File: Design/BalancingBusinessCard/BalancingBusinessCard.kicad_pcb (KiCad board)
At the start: 2 copper layers, 51 x 89 mm, 31 parts, among them J101 TestPoints, M201 Motor_DC, U101 ATtiny261-20SU, U201 AP1017AEN, U401 LIS3DHTR, U501 FT440CA

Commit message: Final from Saturday
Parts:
- U401: value LIS3DHTR -> LGA-16_3x3x1mm

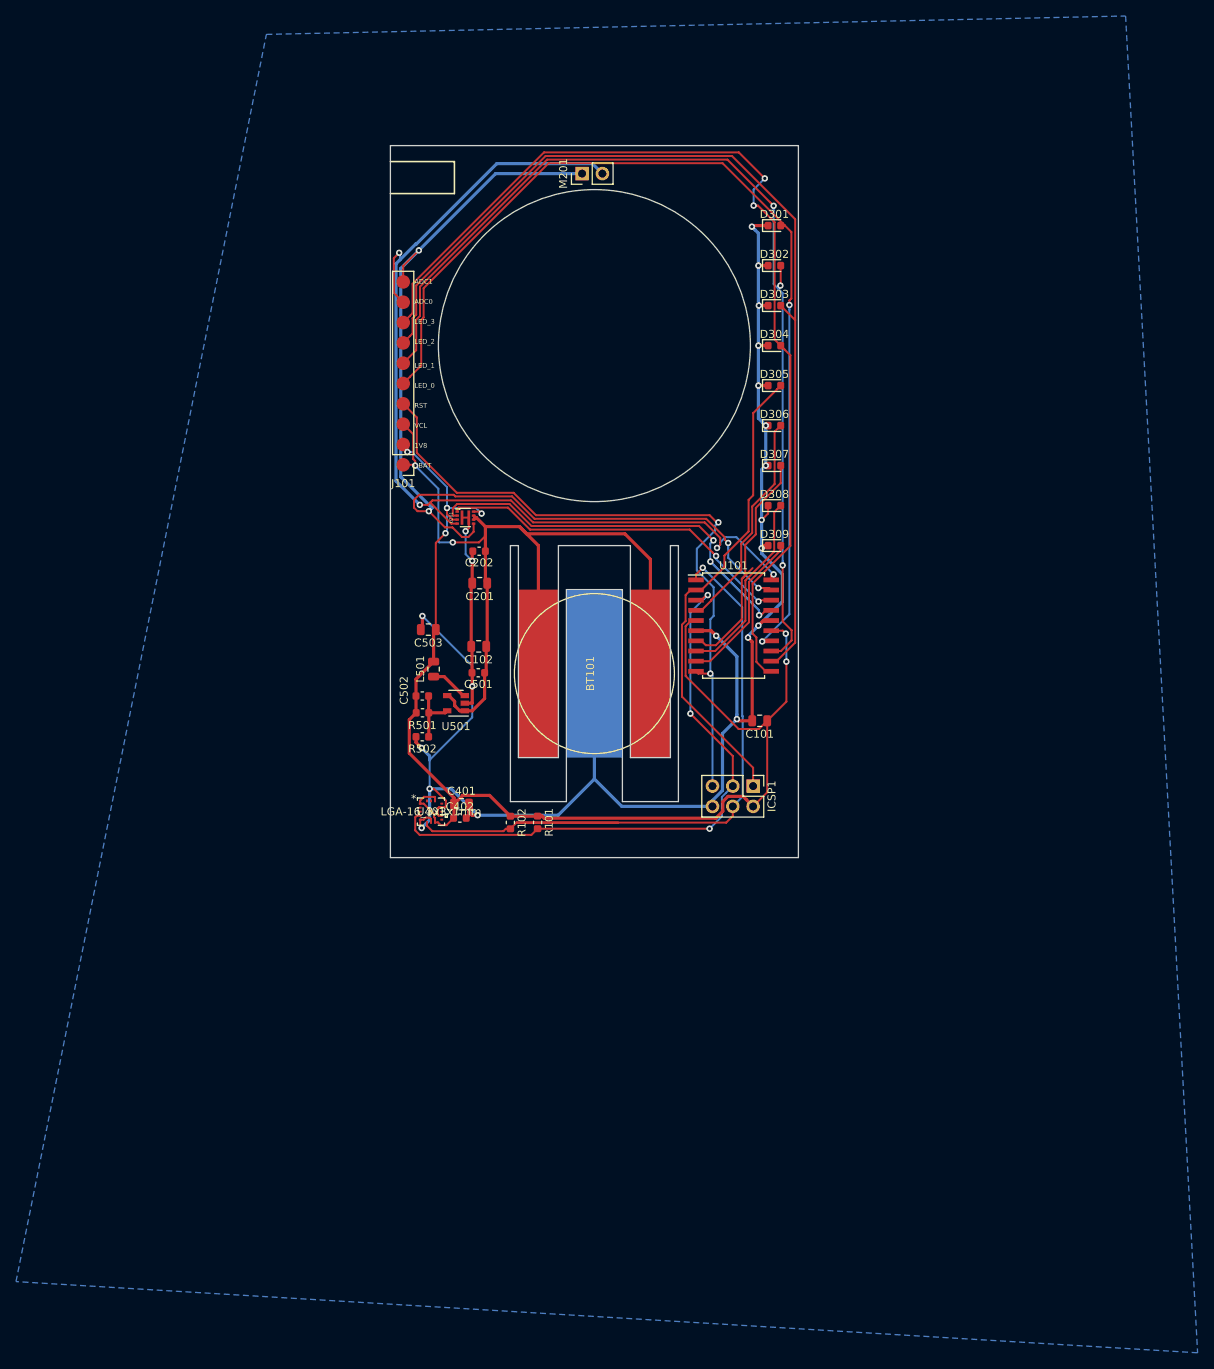
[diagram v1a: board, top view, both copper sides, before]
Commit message: Made mousebites and improved battery tab
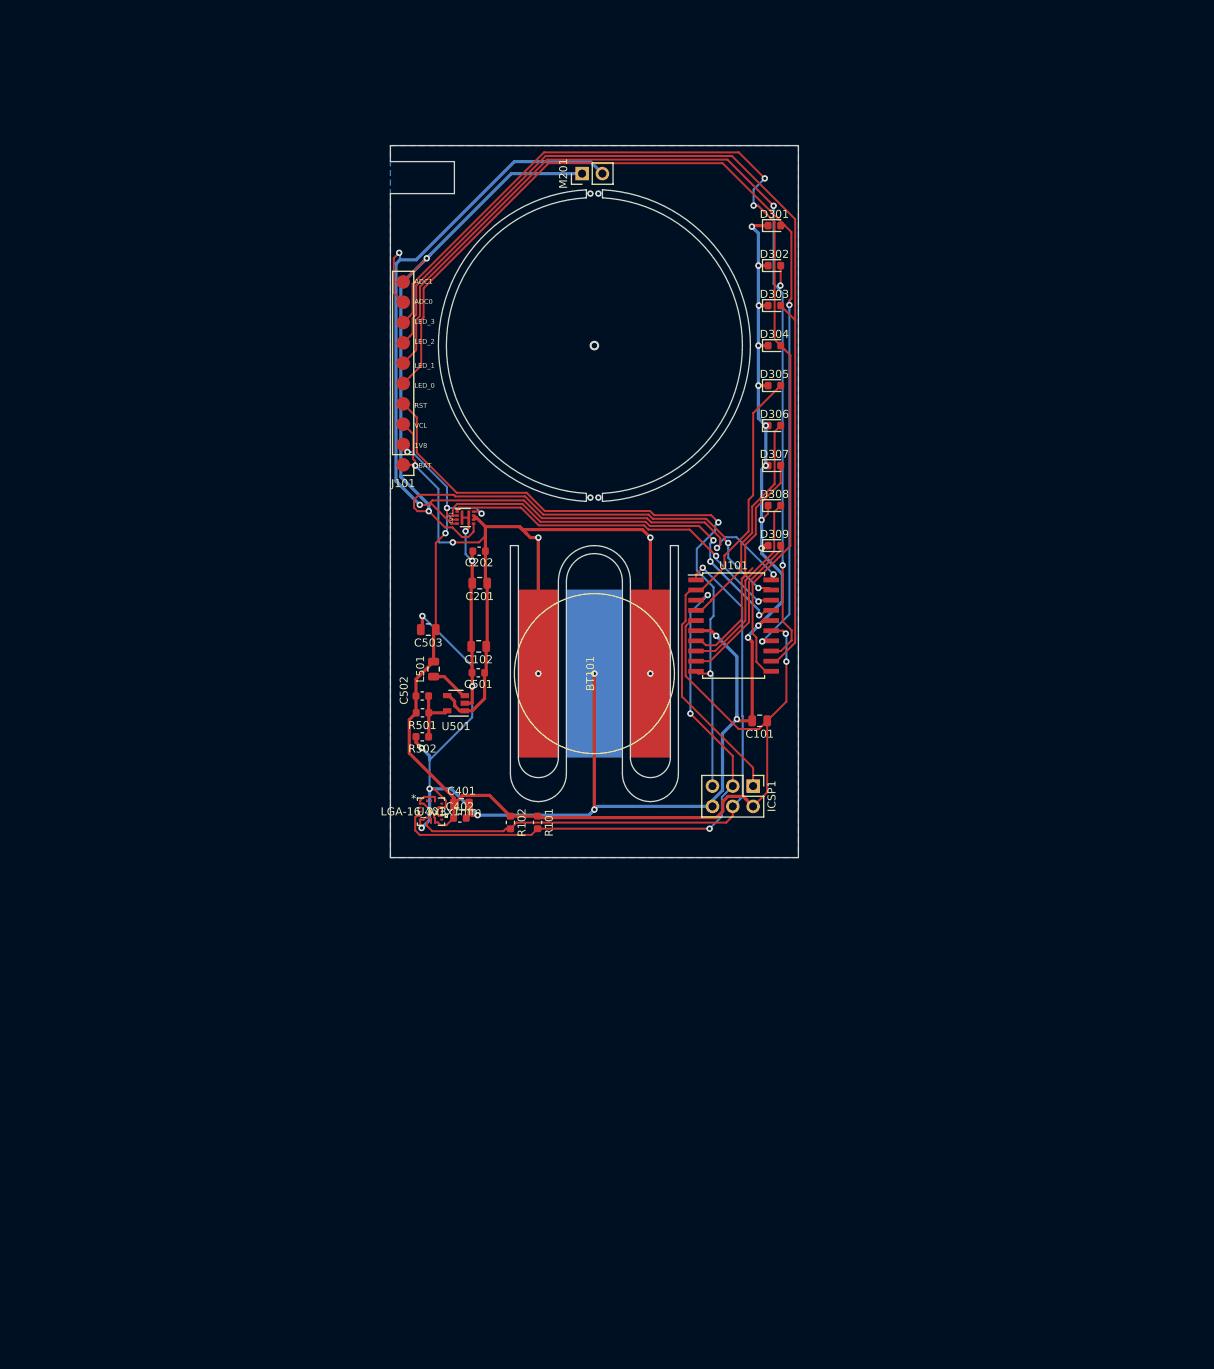
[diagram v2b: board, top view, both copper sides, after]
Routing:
- net +BATT: track 110.6 -> 129.8 mm, vias 2 -> 6
- net GND: track 236.4 -> 254.4 mm, vias 21 -> 23
- net /MOSI: track 87.9 -> 75.2 mm
- net /ADC1: track 126.8 -> 124.7 mm
- net (no net): vias 0 -> 5
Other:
- outline, holes or cut-outs redrawn
